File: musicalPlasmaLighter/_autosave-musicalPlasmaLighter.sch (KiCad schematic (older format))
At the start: 13 parts, among them U1 ATtiny85-20SU, U2 LTC4054ES5-4.2, U3 74HCT00

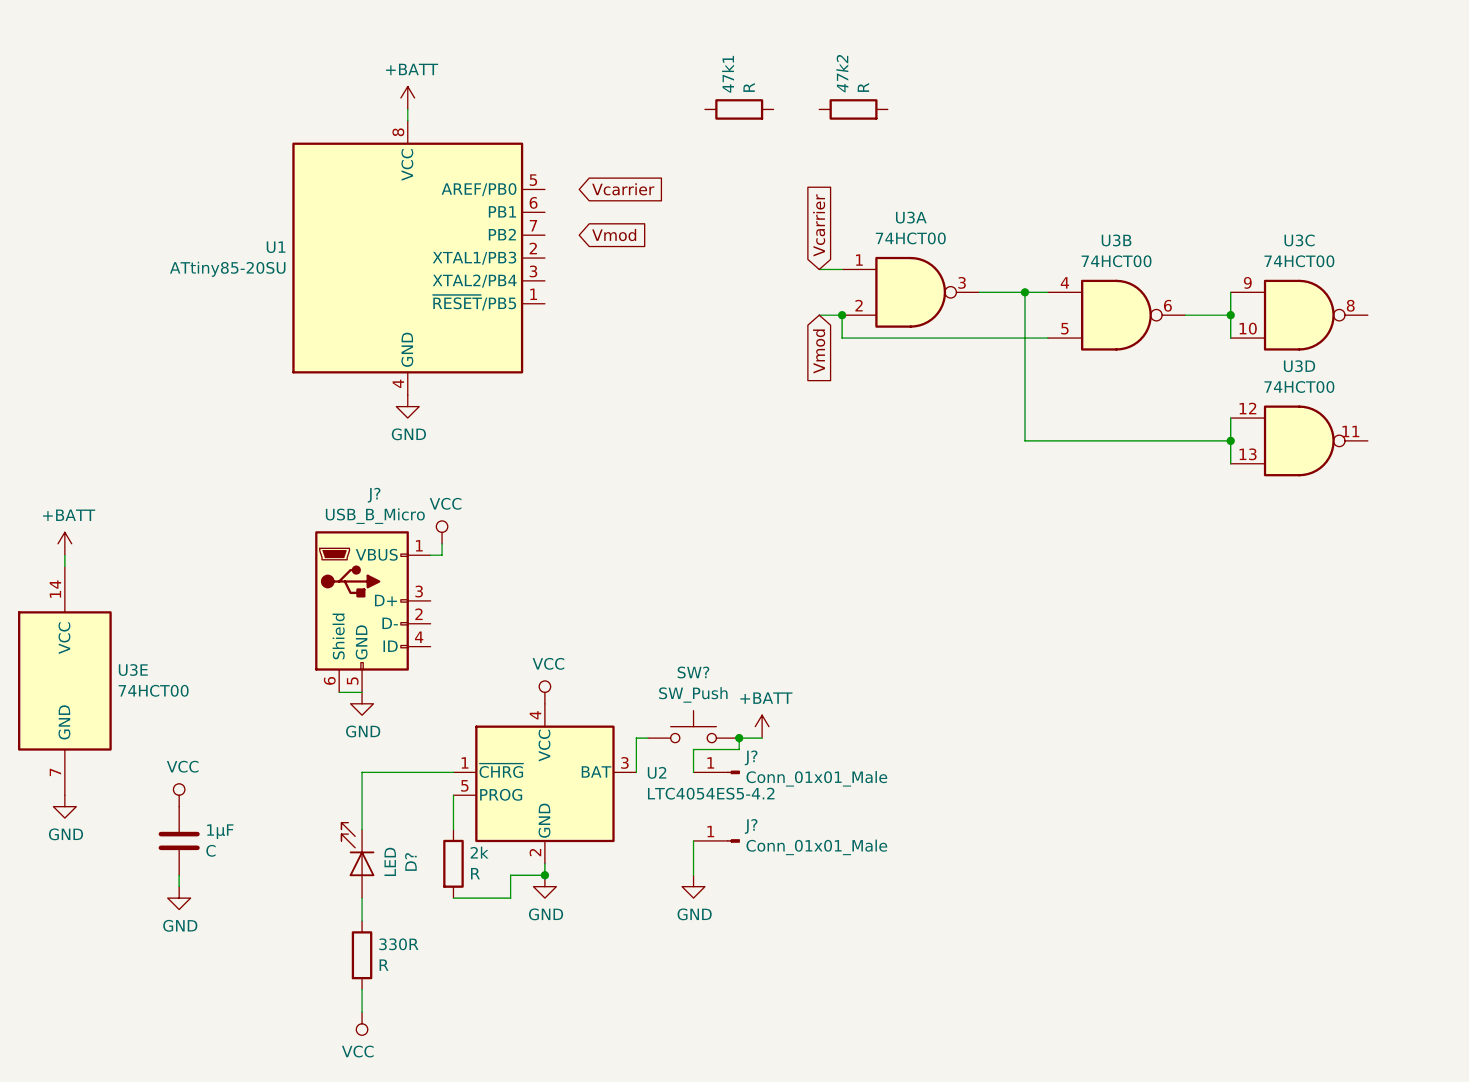
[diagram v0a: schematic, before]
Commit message: updated schematics
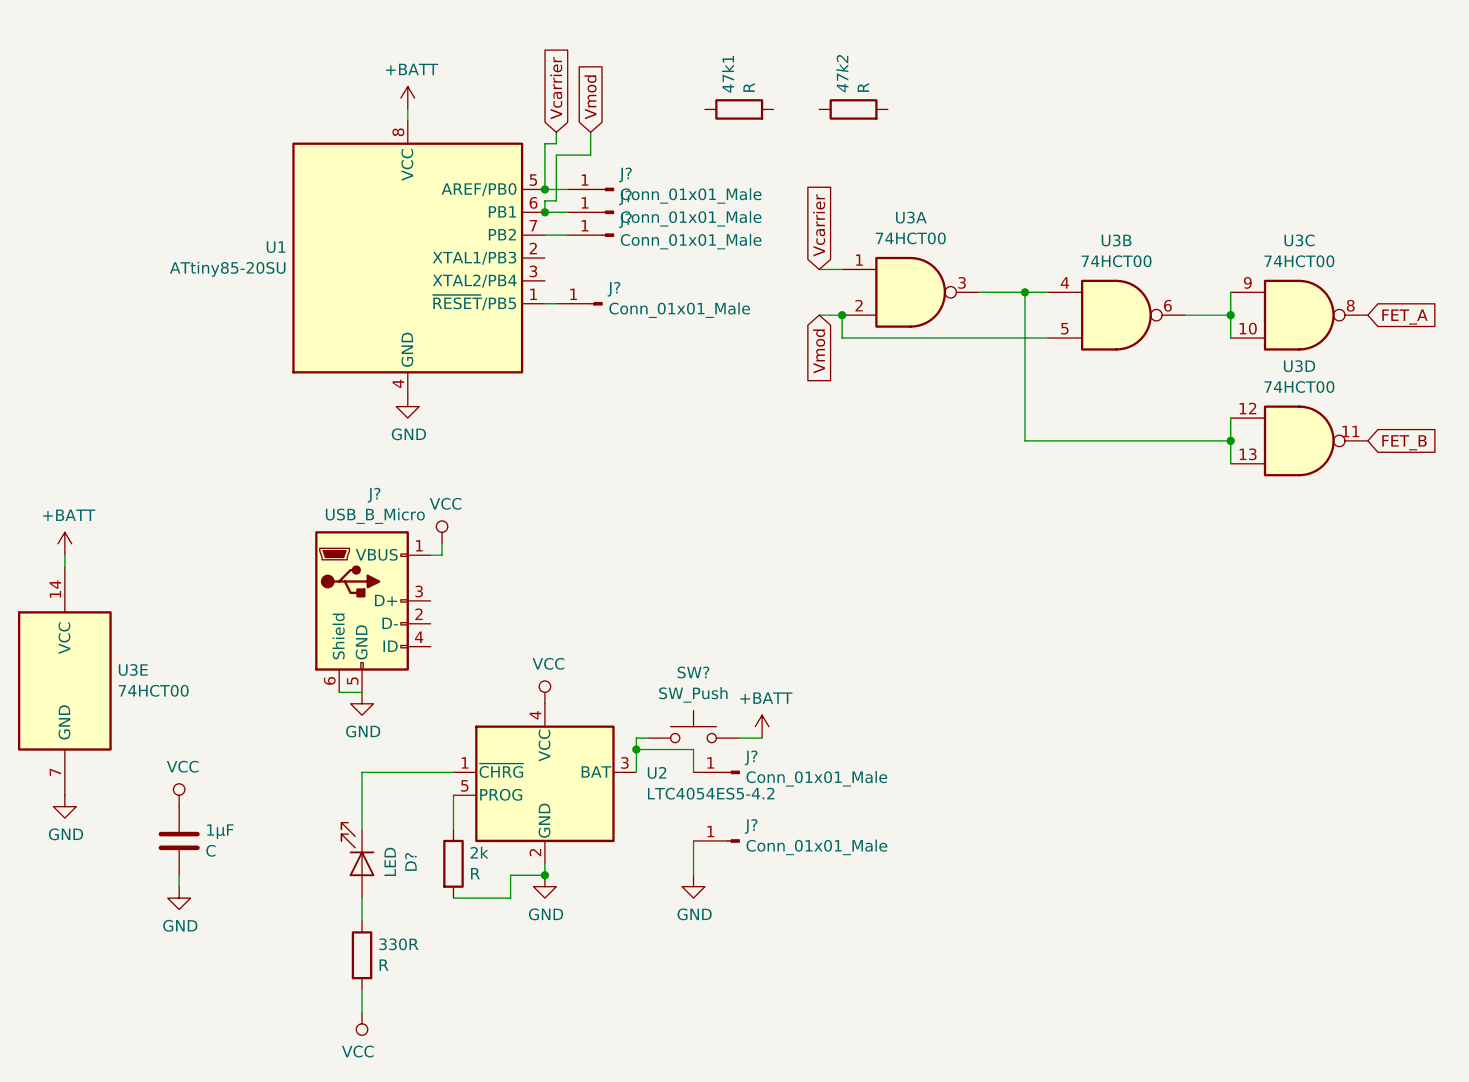
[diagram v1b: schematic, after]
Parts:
- added J? (x4): Conn_01x01_Male, symbol Connector:Conn_01x01_Male
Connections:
- net +BATT: no longer J?.1 (Pin_1)
- net Vcarrier: now also U1.5 (AREF/PB0), J?.1 (Pin_1)
- net Vmod: now also U1.6 (PB1), J?.1 (Pin_1)
- net at U1.1 (~RESET~/PB5): now also J?.1 (Pin_1)
- net at U1.7 (PB2): now also J?.1 (Pin_1)
- net FET_A: now reaches U3.8
- net FET_B: now reaches U3.11
- net at SW?.1, U2.3 (BAT): now also J?.1 (Pin_1)
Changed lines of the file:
@@
 EESchema Schematic File Version 4
+LIBS:musicalPlasmaLighter-cache
 EELAYER 30 0
 EELAYER END
@@
 $EndComp
 Wire Wire Line
-	3700 4000 3700 3850
+	3700 4000 3700 3900
 Wire Wire Line
 	3700 3850 3750 3850
@@
 Wire Wire Line
 	3950 4000 3950 3900
-Wire Wire Line
-	3950 3900 4150 3900
-Wire Wire Line
-	4150 3900 4150 3850
-Connection ~ 4150 3850
 Wire Wire Line
 	3950 4450 3950 4300
@@
 Wire Wire Line
 	4600 1800 4500 1800
-Text GLabel 3450 1450 2    50   Input ~ 0
+Text GLabel 3350 1200 1    50   Input ~ 0
 Vcarrier
-Text GLabel 3450 1650 2    50   Input ~ 0
+Text GLabel 3500 1200 1    50   Input ~ 0
 Vmod
+Text GLabel 6900 2000 2    50   Input ~ 0
+FET_A
+Text GLabel 6900 2550 2    50   Input ~ 0
+FET_B
+Wire Wire Line
+	3950 3900 3700 3900
+Connection ~ 3700 3900
+Wire Wire Line
+	3700 3900 3700 3850
+$Comp
+L Connector:Conn_01x01_Male J?
+U 1 1 5D766EE0
+P 3550 1950
+F 0 "J?" H 3522 1882 50  0000 R CNN
+F 1 "Conn_01x01_Male" H 3522 1973 50  0000 R CNN
+F 2 "" H 3550 1950 50  0001 C CNN
+F 3 "~" H 3550 1950 50  0001 C CNN
+	1    3550 1950
+	-1   0    0    1
+$EndComp
+$Comp
+L Connector:Conn_01x01_Male J?
+U 1 1 5D767EEF
+P 3600 1450
+F 0 "J?" H 3572 1382 50  0000 R CNN
+F 1 "Conn_01x01_Male" H 3572 1473 50  0000 R CNN
+F 2 "" H 3600 1450 50  0001 C CNN
+F 3 "~" H 3600 1450 50  0001 C CNN
+	1    3600 1450
+	-1   0    0    1
+$EndComp
+$Comp
+L Connector:Conn_01x01_Male J?
+U 1 1 5D7685C5
+P 3600 1550
+F 0 "J?" H 3572 1482 50  0000 R CNN
+F 1 "Conn_01x01_Male" H 3572 1573 50  0000 R CNN
+F 2 "" H 3600 1550 50  0001 C CNN
+F 3 "~" H 3600 1550 50  0001 C CNN
+	1    3600 1550
+	-1   0    0    1
+$EndComp
+$Comp
+L Connector:Conn_01x01_Male J?
+U 1 1 5D768DFD
+P 3600 1650
+F 0 "J?" H 3572 1582 50  0000 R CNN
+F 1 "Conn_01x01_Male" H 3572 1673 50  0000 R CNN
+F 2 "" H 3600 1650 50  0001 C CNN
+F 3 "~" H 3600 1650 50  0001 C CNN
+	1    3600 1650
+	-1   0    0    1
+$EndComp
+Wire Wire Line
+	3300 1450 3300 1250
+Wire Wire Line
+	3300 1250 3350 1250
+Wire Wire Line
+	3350 1250 3350 1200
+Wire Wire Line
+	3300 1550 3300 1500
+Wire Wire Line
+	3300 1500 3350 1500
+Wire Wire Line
+	3350 1300 3500 1300
+Wire Wire Line
+	3500 1300 3500 1200
+Wire Wire Line
+	3350 1300 3350 1500
+Wire Wire Line
+	3300 1450 3400 1450
+Connection ~ 3300 1450
+Wire Wire Line
+	3300 1550 3400 1550
+Connection ~ 3300 1550
+Wire Wire Line
+	3300 1650 3400 1650
+Wire Wire Line
+	3350 1950 3300 1950
 $EndSCHEMATC
